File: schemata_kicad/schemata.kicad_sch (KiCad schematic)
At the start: 0 parts

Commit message: pridani textu peak detect, xor phase, signal source
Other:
- added sheet XOR_phase (XOR_phase.kicad_sch)
- added sheet peak_detect (peak_detect.kicad_sch)
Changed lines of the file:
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@@
 	)
 	(sheet
-		(at 46.355 60.96)
-		(size 12.7 3.81)
+		(at 17.145 50.8)
+		(size 24.765 10.16)
 		(exclude_from_sim no)
 		(in_bom yes)
@@
 		)
 		(property "Sheetname" "resonant method"
-			(at 46.355 60.2484 0)
+			(at 17.145 50.0884 0)
 			(effects
 				(font
@@
 		)
 		(property "Sheetfile" "resonant.kicad_sch"
-			(at 46.355 65.3546 0)
+			(at 17.145 61.5446 0)
 			(effects
 				(font
@@
 				)
 			)
+		)
+	)
+	(sheet
+		(at 17.78 90.17)
+		(size 24.13 8.89)
+		(exclude_from_sim no)
+		(in_bom yes)
+		(on_board yes)
+		(dnp no)
+		(fields_autoplaced yes)
+		(stroke
+			(width 0.1524)
+			(type solid)
+		)
+		(fill
+			(color 0 0 0 0.0000)
+		)
+		(property "Sheetname" "XOR_phase"
+			(at 17.78 89.4584 0)
+			(effects
+				(font
+					(size 1.27 1.27)
+				)
+				(justify left bottom)
+			)
+		)
+		(property "Sheetfile" "XOR_phase.kicad_sch"
+			(at 17.78 99.6446 0)
+			(effects
+				(font
+					(size 1.27 1.27)
+				)
+				(justify left top)
+			)
+		)
+		(instances
+			(project "schemata"
+				(path "/ba5b7f3f-bcc2-4274-bf72-d951c4da15c7"
+					(page "6")
+				)
+			)
+		)
+	)
+	(sheet
+		(at 17.78 71.12)
+		(size 24.13 8.89)
+		(exclude_from_sim no)
+		(in_bom yes)
+		(on_board yes)
+		(dnp no)
+		(fields_autoplaced yes)
+		(stroke
+			(width 0.1524)
+			(type solid)
+		)
+		(fill
+			(color 0 0 0 0.0000)
+		)
+		(property "Sheetname" "peak_detect"
+			(at 17.78 70.4084 0)
+			(effects
+				(font
+					(size 1.27 1.27)
+				)
+				(justify left bottom)
+			)
+		)
+		(property "Sheetfile" "peak_detect.kicad_sch"
+			(at 17.78 80.5946 0)
+			(effects
+				(font
+					(size 1.27 1.27)
+				)
+				(justify left top)
+			)
+		)
+		(instances
+			(project "schemata"
+				(path "/ba5b7f3f-bcc2-4274-bf72-d951c4da15c7"
+					(page "5")
+				)
+			)

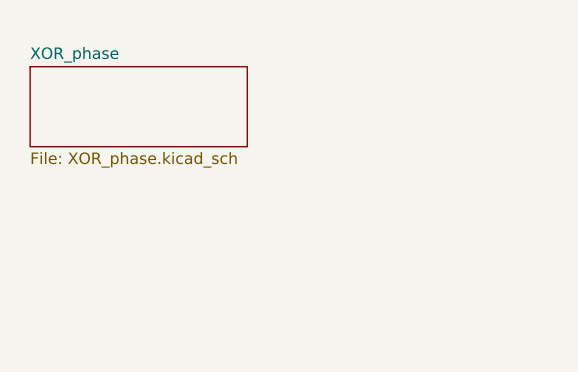
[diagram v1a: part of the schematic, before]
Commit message: update rizeni amplitudy
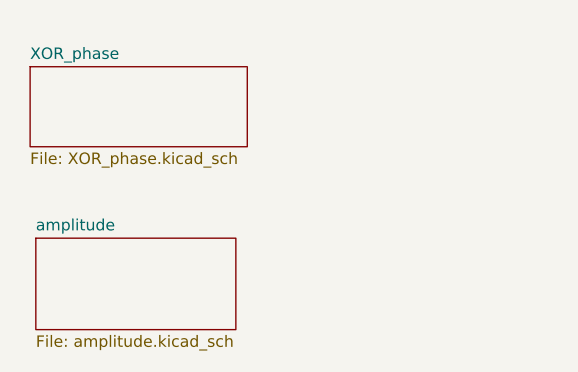
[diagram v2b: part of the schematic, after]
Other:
- added sheet amplitude (amplitude.kicad_sch)
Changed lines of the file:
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@@
+	)
+	(sheet
+		(at 18.415 109.22)
+		(size 22.225 10.16)
+		(exclude_from_sim no)
+		(in_bom yes)
+		(on_board yes)
+		(dnp no)
+		(fields_autoplaced yes)
+		(stroke
+			(width 0.1524)
+			(type solid)
+		)
+		(fill
+			(color 0 0 0 0.0000)
+		)
+		(property "Sheetname" "amplitude"
+			(at 18.415 108.5084 0)
+			(effects
+				(font
+					(size 1.27 1.27)
+				)
+				(justify left bottom)
+			)
+		)
+		(property "Sheetfile" "amplitude.kicad_sch"
+			(at 18.415 119.9646 0)
+			(effects
+				(font
+					(size 1.27 1.27)
+				)
+				(justify left top)
+			)
+		)
+		(instances
+			(project "schemata"
+				(path "/ba5b7f3f-bcc2-4274-bf72-d951c4da15c7"
+					(page "7")
+				)
+			)
+		)
 	)
 	(sheet

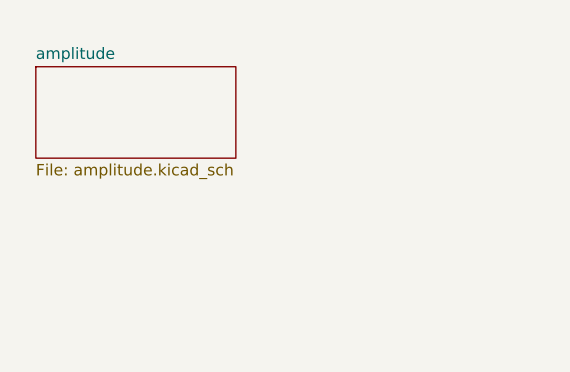
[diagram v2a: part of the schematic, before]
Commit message: pridane nastaveni dc offsetu do zdroje a neco ke vzorkovani
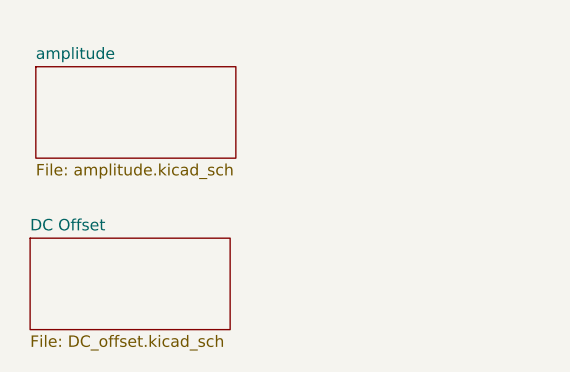
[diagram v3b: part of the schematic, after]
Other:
- added sheet DC Offset (DC_offset.kicad_sch)
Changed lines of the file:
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@@
+	)
+	(sheet
+		(at 17.78 128.27)
+		(size 22.225 10.16)
+		(exclude_from_sim no)
+		(in_bom yes)
+		(on_board yes)
+		(dnp no)
+		(fields_autoplaced yes)
+		(stroke
+			(width 0.1524)
+			(type solid)
+		)
+		(fill
+			(color 0 0 0 0.0000)
+		)
+		(property "Sheetname" "DC Offset"
+			(at 17.78 127.5584 0)
+			(effects
+				(font
+					(size 1.27 1.27)
+				)
+				(justify left bottom)
+			)
+		)
+		(property "Sheetfile" "DC_offset.kicad_sch"
+			(at 17.78 139.0146 0)
+			(effects
+				(font
+					(size 1.27 1.27)
+				)
+				(justify left top)
+			)
+		)
+		(instances
+			(project "schemata"
+				(path "/ba5b7f3f-bcc2-4274-bf72-d951c4da15c7"
+					(page "8")
+				)
+			)
+		)
 	)
 	(sheet

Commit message: update
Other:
- added sheet range_switch (range_switch.kicad_sch)
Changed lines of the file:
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@@
 (kicad_sch
-	(version 20250114)
+	(version 20260306)
 	(generator "eeschema")
-	(generator_version "9.0")
+	(generator_version "10.0")
 	(paper "A4")
 	(text "Ix"
@@
 	)
 	(sheet
+		(at 48.26 17.78)
+		(size 29.21 8.89)
+		(exclude_from_sim no)
+		(in_bom yes)
+		(on_board yes)
+		(dnp no)
+		(fields_autoplaced yes)
+		(stroke
+			(width 0.1524)
+			(type solid)
+		)
+		(fill
+			(color 0 0 0 0)
+		)
+		(property "Sheetname" "range_switch"
+			(at 48.26 17.0684 0)
+			(show_name no)
+			(do_not_autoplace no)
+			(effects
+				(font
+					(size 1.27 1.27)
+				)
+				(justify left bottom)
+			)
+		)
+		(property "Sheetfile" "range_switch.kicad_sch"
+			(at 48.26 27.2546 0)
+			(show_name no)
+			(do_not_autoplace no)
+			(effects
+				(font
+					(size 1.27 1.27)
+				)
+				(justify left top)
+			)
+		)
+		(instances
+			(project "schemata"
+				(path "/ba5b7f3f-bcc2-4274-bf72-d951c4da15c7"
+					(page "9")
+				)
+			)
+		)
+	)
+	(sheet
 		(at 16.51 16.51)
 		(size 25.4 8.89)
@@
 		)
 		(fill
-			(color 0 0 0 0.0000)
+			(color 0 0 0 0)
 		)
 		(property "Sheetname" "i_v_conv"
 			(at 16.51 15.7984 0)
+			(show_name no)
+			(do_not_autoplace no)
 			(effects
 				(font
@@
 		(property "Sheetfile" "i_v_conv.kicad_sch"
 			(at 16.51 25.9846 0)
+			(show_name no)
+			(do_not_autoplace no)
 			(effects
 				(font
@@
 		)
 		(fill
-			(color 0 0 0 0.0000)
+			(color 0 0 0 0)
 		)
 		(property "Sheetname" "resonant method"
 			(at 17.145 50.0884 0)
+			(show_name no)
+			(do_not_autoplace no)
 			(effects
 				(font
@@
 		(property "Sheetfile" "resonant.kicad_sch"
 			(at 17.145 61.5446 0)
+			(show_name no)
+			(do_not_autoplace no)
 			(effects
 				(font
@@
 		)
 		(fill
-			(color 0 0 0 0.0000)
+			(color 0 0 0 0)
 		)
 		(property "Sheetname" "DC Offset"
 			(at 17.78 127.5584 0)
+			(show_name no)
+			(do_not_autoplace no)
 			(effects
 				(font
@@
 		(property "Sheetfile" "DC_offset.kicad_sch"
 			(at 17.78 139.0146 0)
+			(show_name no)
+			(do_not_autoplace no)
 			(effects
 				(font
@@
 		)
 		(fill
-			(color 0 0 0 0.0000)
+			(color 0 0 0 0)
 		)
 		(property "Sheetname" "XOR_phase"
 			(at 17.78 89.4584 0)
+			(show_name no)
+			(do_not_autoplace no)
 			(effects
 				(font
@@
 		(property "Sheetfile" "XOR_phase.kicad_sch"
 			(at 17.78 99.6446 0)
+			(show_name no)
+			(do_not_autoplace no)
 			(effects
 				(font
@@
 		)
 		(fill
-			(color 0 0 0 0.0000)
+			(color 0 0 0 0)
 		)
 		(property "Sheetname" "amplitude"
 			(at 18.415 108.5084 0)
+			(show_name no)
+			(do_not_autoplace no)
 			(effects
 				(font
@@
 		(property "Sheetfile" "amplitude.kicad_sch"
 			(at 18.415 119.9646 0)
+			(show_name no)
+			(do_not_autoplace no)
 			(effects
 				(font
@@
 		)
 		(fill
-			(color 0 0 0 0.0000)
+			(color 0 0 0 0)
 		)
 		(property "Sheetname" "peak_detect"
 			(at 17.78 70.4084 0)
+			(show_name no)
+			(do_not_autoplace no)
 			(effects
 				(font
@@
 		(property "Sheetfile" "peak_detect.kicad_sch"
 			(at 17.78 80.5946 0)
+			(show_name no)
+			(do_not_autoplace no)
 			(effects
 				(font
@@
 		)
 		(fill
-			(color 0 0 0 0.0000)
+			(color 0 0 0 0)
 		)
 		(property "Sheetname" "wheatstone"
 			(at 16.51 32.3084 0)
+			(show_name no)
+			(do_not_autoplace no)
 			(effects
 				(font
@@
 		(property "Sheetfile" "wheatstone.kicad_sch"
 			(at 16.51 42.4946 0)
-			(effects
-				(font
+			(show_name no)
+			(do_not_autoplace no)
+			(effects
+				(font

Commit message: 4wire a dalsi
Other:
- added sheet i_v_conv1 (i_v_conv.kicad_sch)
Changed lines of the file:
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@@
+		)
+	)
+	(sheet
+		(at 52.07 35.56)
+		(size 25.4 8.89)
+		(exclude_from_sim no)
+		(in_bom yes)
+		(on_board yes)
+		(dnp no)
+		(fields_autoplaced yes)
+		(stroke
+			(width 0.1524)
+			(type solid)
+		)
+		(fill
+			(color 0 0 0 0)
+		)
+		(property "Sheetname" "i_v_conv1"
+			(at 52.07 34.8484 0)
+			(show_name no)
+			(do_not_autoplace no)
+			(effects
+				(font
+					(size 1.27 1.27)
+				)
+				(justify left bottom)
+			)
+		)
+		(property "Sheetfile" "i_v_conv.kicad_sch"
+			(at 52.07 45.0346 0)
+			(show_name no)
+			(do_not_autoplace no)
+			(effects
+				(font
+					(size 1.27 1.27)
+				)
+				(justify left top)
+			)
+		)
+		(instances
+			(project "schemata"
+				(path "/ba5b7f3f-bcc2-4274-bf72-d951c4da15c7"
+					(page "10")
+				)
+			)
 		)
 	)

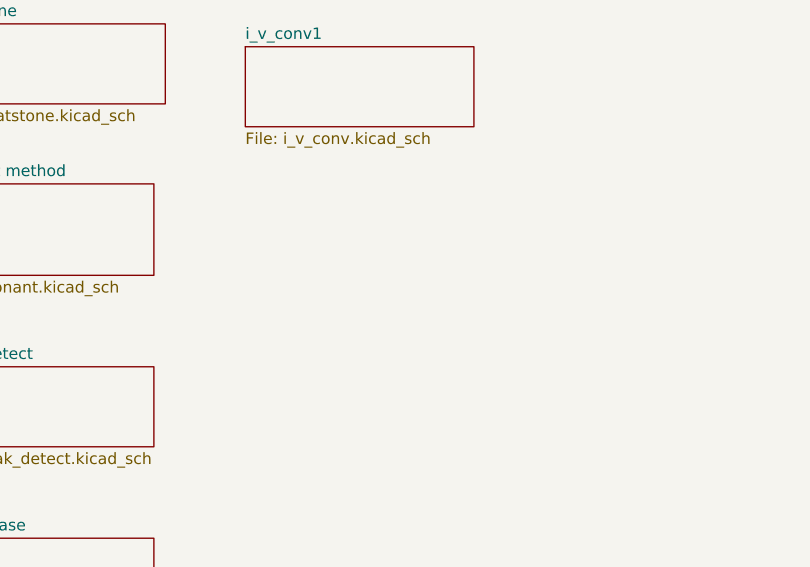
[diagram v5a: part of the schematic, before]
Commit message: nejake edity vysledku a kompenzace seriovym rezistorem
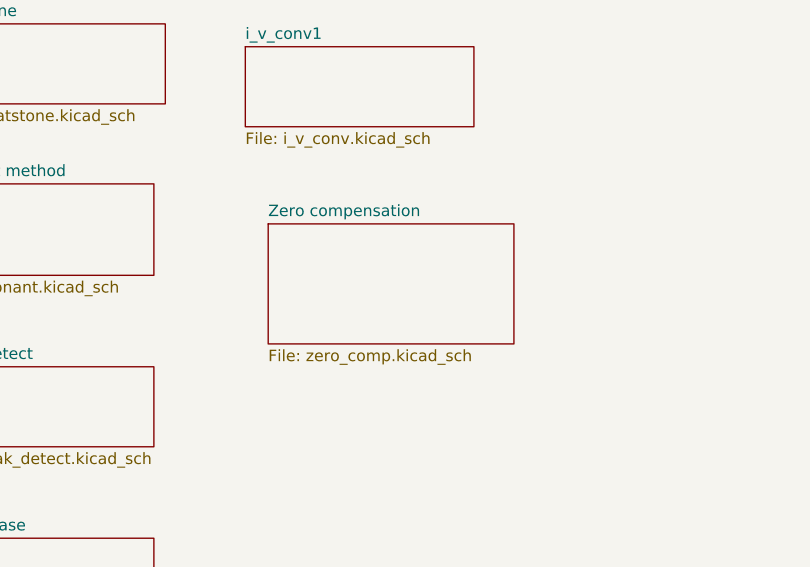
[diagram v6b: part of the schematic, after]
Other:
- added sheet Zero compensation (zero_comp.kicad_sch)
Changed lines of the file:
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@@
+	)
+	(sheet
+		(at 54.61 55.245)
+		(size 27.305 13.335)
+		(exclude_from_sim no)
+		(in_bom yes)
+		(on_board yes)
+		(dnp no)
+		(fields_autoplaced yes)
+		(stroke
+			(width 0.1524)
+			(type solid)
+		)
+		(fill
+			(color 0 0 0 0)
+		)
+		(property "Sheetname" "Zero compensation"
+			(at 54.61 54.5334 0)
+			(show_name no)
+			(do_not_autoplace no)
+			(effects
+				(font
+					(size 1.27 1.27)
+				)
+				(justify left bottom)
+			)
+		)
+		(property "Sheetfile" "zero_comp.kicad_sch"
+			(at 54.61 69.1646 0)
+			(show_name no)
+			(do_not_autoplace no)
+			(effects
+				(font
+					(size 1.27 1.27)
+				)
+				(justify left top)
+			)
+		)
+		(instances
+			(project "schemata"
+				(path "/ba5b7f3f-bcc2-4274-bf72-d951c4da15c7"
+					(page "11")
+				)
+			)
+		)
 	)
 	(sheet
